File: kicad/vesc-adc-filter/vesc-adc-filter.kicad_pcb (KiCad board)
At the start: 2 copper layers, 51 x 12 mm, 7 parts, among them J1 PWM

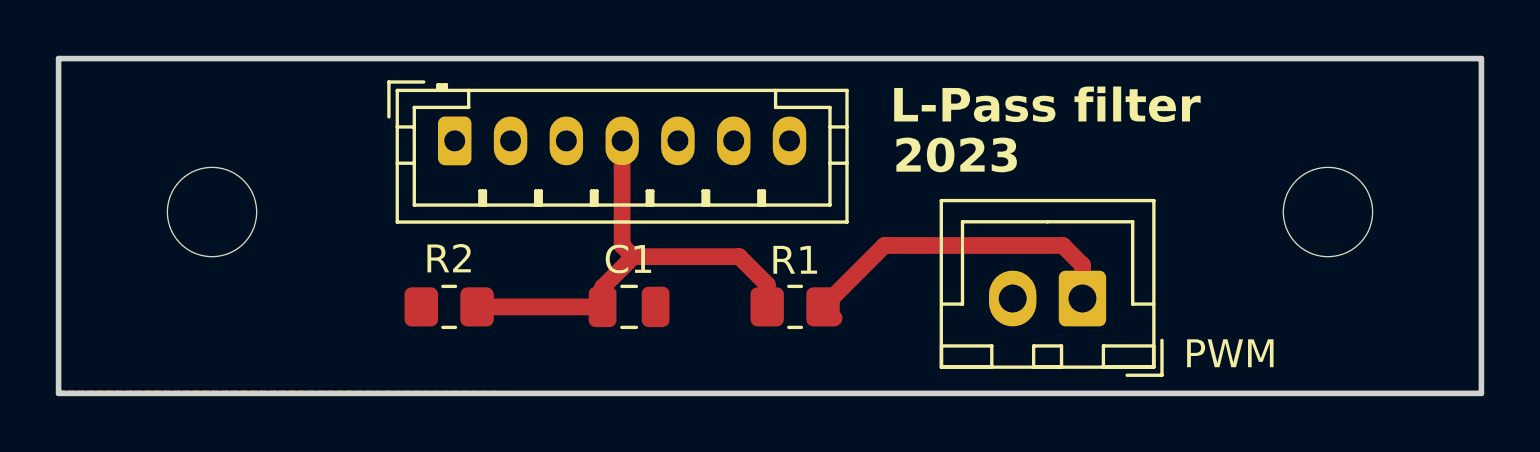
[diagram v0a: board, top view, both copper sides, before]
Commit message: Added encoder breakout and updated other projects
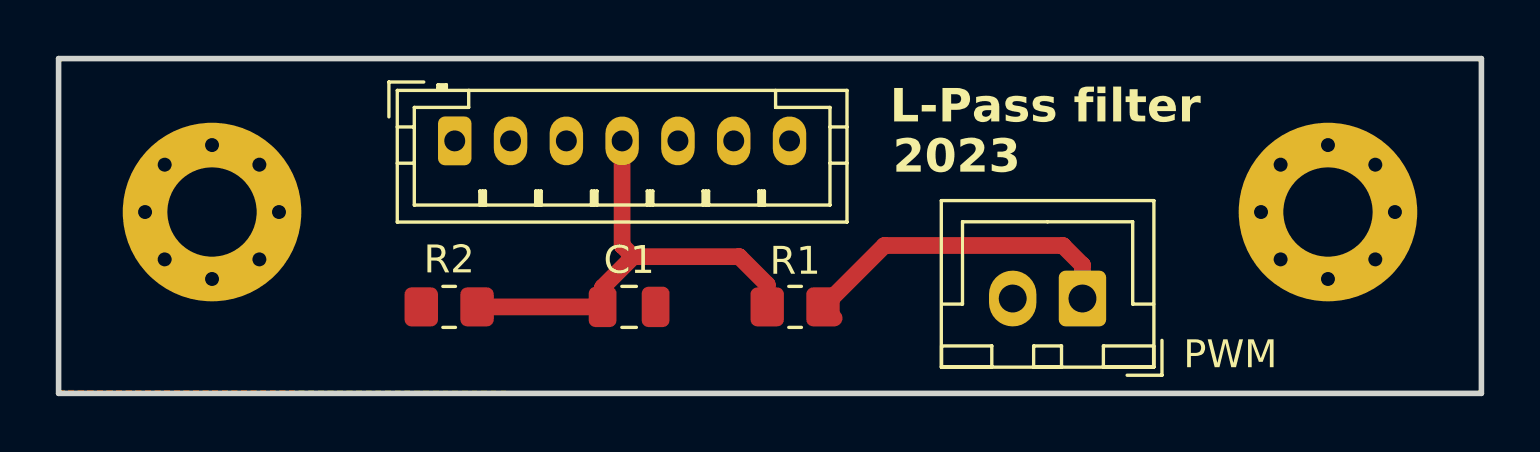
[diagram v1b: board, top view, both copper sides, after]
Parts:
- H1, H2: footprint MountingHole:MountingHole_3.2mm_M3 -> MountingHole:MountingHole_3.2mm_M3_Pad_Via
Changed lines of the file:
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@@
     )
   )
-  (footprint "MountingHole:MountingHole_3.2mm_M3" (layer "F.Cu")
+  (footprint "MountingHole:MountingHole_3.2mm_M3_Pad_Via" (layer "F.Cu")
     (at 74.5 65)
-    (descr "Mounting Hole 3.2mm, no annular, M3")
-    (tags "mounting hole 3.2mm no annular m3")
+    (descr "Mounting Hole 3.2mm, M3")
+    (tags "mounting hole 3.2mm m3")
     (property "Sheetfile" "vesc-adc-filter.kicad_sch")
     (property "Sheetname" "")
@@
     (fp_circle (center 0 0) (end 3.45 0)
       (stroke (width 0.05) (type solid)) (fill none) (layer "F.CrtYd"))
-    (pad "" np_thru_hole circle (at 0 0) (size 3.2 3.2) (drill 3.2) (layers "*.Cu" "*.Mask"))
+    (pad "1" thru_hole circle (at -2.4 0) (size 0.8 0.8) (drill 0.5) (layers "*.Cu" "*.Mask"))
+    (pad "1" thru_hole circle (at -1.697056 -1.697056) (size 0.8 0.8) (drill 0.5) (layers "*.Cu" "*.Mask"))
+    (pad "1" thru_hole circle (at -1.697056 1.697056) (size 0.8 0.8) (drill 0.5) (layers "*.Cu" "*.Mask"))
+    (pad "1" thru_hole circle (at 0 -2.4) (size 0.8 0.8) (drill 0.5) (layers "*.Cu" "*.Mask"))
+    (pad "1" thru_hole circle (at 0 0) (size 6.4 6.4) (drill 3.2) (layers "*.Cu" "*.Mask"))
+    (pad "1" thru_hole circle (at 0 2.4) (size 0.8 0.8) (drill 0.5) (layers "*.Cu" "*.Mask"))
+    (pad "1" thru_hole circle (at 1.697056 -1.697056) (size 0.8 0.8) (drill 0.5) (layers "*.Cu" "*.Mask"))
+    (pad "1" thru_hole circle (at 1.697056 1.697056) (size 0.8 0.8) (drill 0.5) (layers "*.Cu" "*.Mask"))
+    (pad "1" thru_hole circle (at 2.4 0) (size 0.8 0.8) (drill 0.5) (layers "*.Cu" "*.Mask"))
   )
-  (footprint "MountingHole:MountingHole_3.2mm_M3" (layer "F.Cu")
+  (footprint "MountingHole:MountingHole_3.2mm_M3_Pad_Via" (layer "F.Cu")
     (at 114.5 65)
-    (descr "Mounting Hole 3.2mm, no annular, M3")
-    (tags "mounting hole 3.2mm no annular m3")
+    (descr "Mounting Hole 3.2mm, M3")
+    (tags "mounting hole 3.2mm m3")
     (property "Sheetfile" "vesc-adc-filter.kicad_sch")
     (property "Sheetname" "")
@@
     (fp_circle (center 0 0) (end 3.45 0)
       (stroke (width 0.05) (type solid)) (fill none) (layer "F.CrtYd"))
-    (pad "" np_thru_hole circle (at 0 0) (size 3.2 3.2) (drill 3.2) (layers "*.Cu" "*.Mask"))
+    (pad "1" thru_hole circle (at -2.4 0) (size 0.8 0.8) (drill 0.5) (layers "*.Cu" "*.Mask"))
+    (pad "1" thru_hole circle (at -1.697056 -1.697056) (size 0.8 0.8) (drill 0.5) (layers "*.Cu" "*.Mask"))
+    (pad "1" thru_hole circle (at -1.697056 1.697056) (size 0.8 0.8) (drill 0.5) (layers "*.Cu" "*.Mask"))
+    (pad "1" thru_hole circle (at 0 -2.4) (size 0.8 0.8) (drill 0.5) (layers "*.Cu" "*.Mask"))
+    (pad "1" thru_hole circle (at 0 0) (size 6.4 6.4) (drill 3.2) (layers "*.Cu" "*.Mask"))
+    (pad "1" thru_hole circle (at 0 2.4) (size 0.8 0.8) (drill 0.5) (layers "*.Cu" "*.Mask"))
+    (pad "1" thru_hole circle (at 1.697056 -1.697056) (size 0.8 0.8) (drill 0.5) (layers "*.Cu" "*.Mask"))
+    (pad "1" thru_hole circle (at 1.697056 1.697056) (size 0.8 0.8) (drill 0.5) (layers "*.Cu" "*.Mask"))
+    (pad "1" thru_hole circle (at 2.4 0) (size 0.8 0.8) (drill 0.5) (layers "*.Cu" "*.Mask"))
   )
   (footprint "Connector_JST:JST_XH_B2B-XH-A_1x02_P2.50mm_Vertical" (layer "F.Cu")
